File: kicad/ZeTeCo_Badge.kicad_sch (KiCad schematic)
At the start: 118 parts, among them J1 GPIO, J12 Bat. (+), J13 Bat. (-), J15 USB_A, J2 3V, Q1 2N7002, Q2 2N7002, Q3 2N7002, Q4 2N7002, U1 ATTINY85-20S

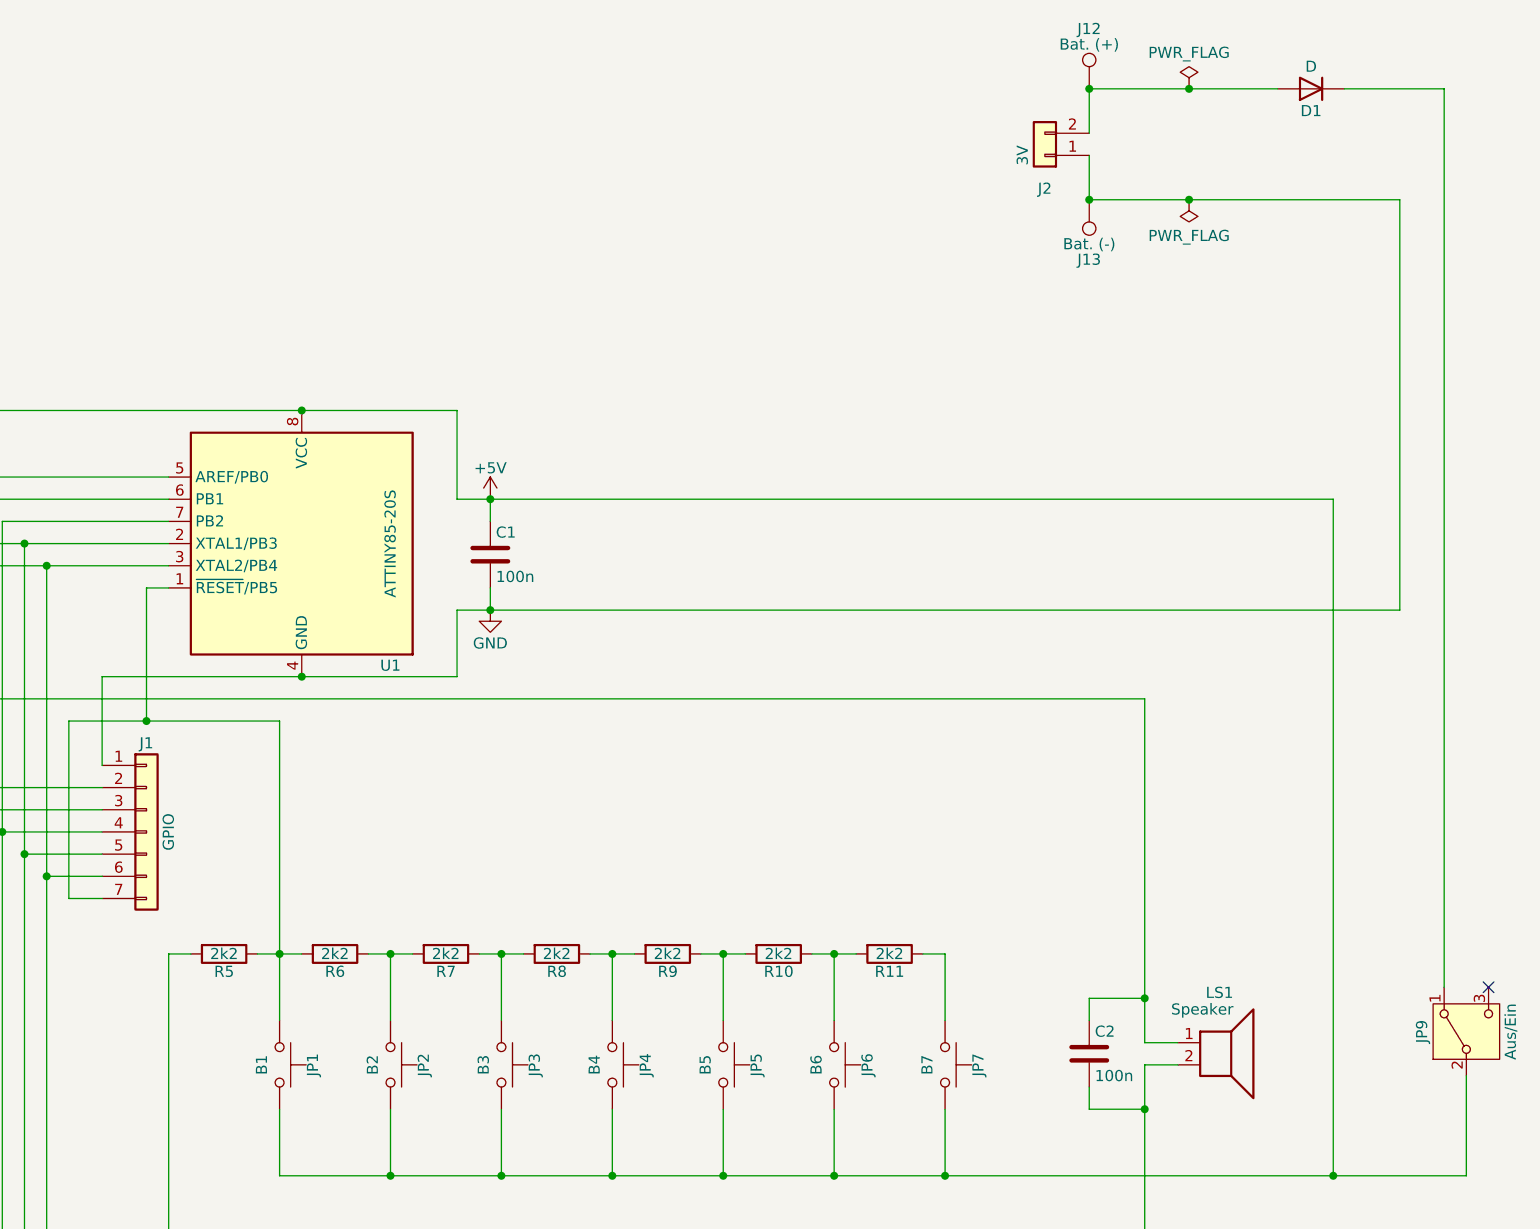
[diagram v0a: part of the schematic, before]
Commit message: Replace PCB text with component values on silkscreen
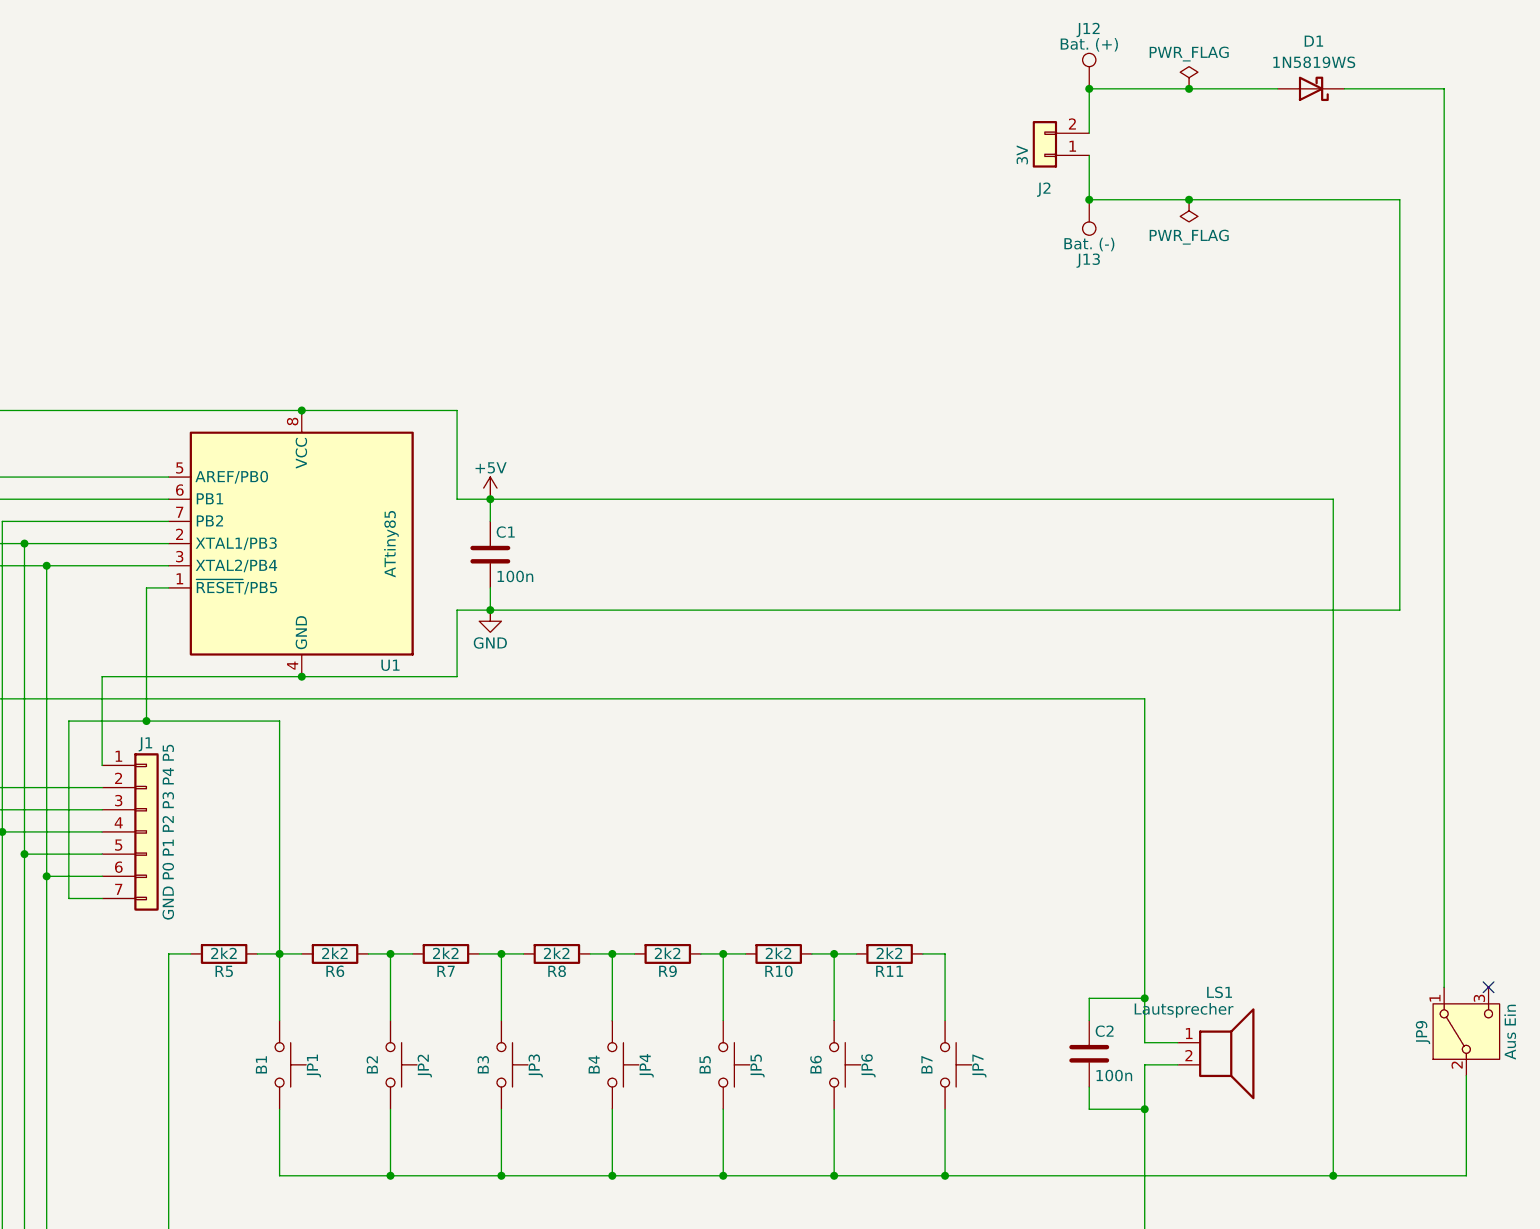
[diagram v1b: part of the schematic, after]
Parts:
- removed D1: D, Diode_SMD:D_1206_3216Metric_Pad1.42x1.75mm_HandSolder, symbol Device:D
- added D1: 1N5819WS, Diode_SMD:D_1206_3216Metric_Pad1.42x1.75mm_HandSolder, symbol Diode:1N5819WS
- J1: value GPIO -> GND P0 P1 P2 P3 P4 P5
- JP9: value Aus/Ein -> Aus Ein
- LS1: value Speaker -> Lautsprecher
- U1: value ATTINY85-20S -> ATtiny85
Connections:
- net at J12.1, J2.2 (Pin_2): now also D1.2 (A)
- net at JP9.1 (A): now also D1.1 (K)
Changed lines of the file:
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@@
 			)
 		)
-		(property "Value" "ATTINY85-20S"
+		(property "Value" "ATtiny85"
 			(at 267.97 83.82 90)
 			(effects
@@
 			)
 		)
-		(property "Value" "Speaker"
+		(property "Value" "Lautsprecher"
 			(at 364.49 137.16 0)
 			(effects
@@
 			)
 		)
-		(property "Value" "Aus/Ein"
+		(property "Value" "Aus    Ein"
 			(at 396.24 139.7 0)
 			(effects
@@
 	)
 	(symbol
-		(lib_id "Device:D")
-		(at 373.38 31.75 180)
-		(unit 1)
-		(exclude_from_sim no)
-		(in_bom yes)
-		(on_board yes)
-		(dnp no)
-		(property "Reference" "D1"
-			(at 373.38 34.29 0)
-			(effects
-				(font
-					(size 1.27 1.27)
-				)
-			)
-		)
-		(property "Value" "D"
-			(at 373.38 29.21 0)
-			(effects
-				(font
-					(size 1.27 1.27)
-				)
-			)
-		)
-		(property "Footprint" "Diode_SMD:D_1206_3216Metric_Pad1.42x1.75mm_HandSolder"
-			(at 373.38 31.75 0)
-			(effects
-				(font
-					(size 1.27 1.27)
-				)
-				(hide yes)
-			)
-		)
-		(property "Datasheet" ""
-			(at 373.38 31.75 0)
-			(effects
-				(font
-					(size 1.27 1.27)
-				)
-				(hide yes)
-			)
-		)
-		(property "Description" "Diode"
-			(at 373.38 31.75 0)
-			(effects
-				(font
-					(size 1.27 1.27)
-				)
-				(hide yes)
-			)
-		)
-		(property "Sim.Device" "D"
-			(at 373.38 31.75 0)
-			(effects
-				(font
-					(size 1.27 1.27)
-				)
-				(hide yes)
-			)
-		)
-		(property "Sim.Pins" "1=K 2=A"
-			(at 373.38 31.75 0)
-			(effects
-				(font
-					(size 1.27 1.27)
-				)
-				(hide yes)
-			)
-		)
-		(pin "2"
-		)
-		(pin "1"
-		)
-		(instances
-			(project ""
-				(path "/1ad60c3f-1b07-4916-ad93-138759b1bafa"
-					(reference "D1")
-					(unit 1)
-				)
-			)
-		)
-	)
-	(symbol
 		(lib_id "Device:C")
 		(at 279.4 85.09 0)
@@
 			)
 		)
-		(property "Value" "GPIO"
+		(property "Value" "GND P0 P1 P2 P3 P4 P5"
 			(at 242.57 116.84 90)
 			(effects
@@
 					(unit 1)
 				)
+			)
+		)
+	)
+	(symbol
+		(lib_id "Diode:1N5819WS")
+		(at 373.38 31.75 180)
+		(unit 1)
+		(exclude_from_sim no)
+		(in_bom yes)
+		(on_board yes)
+		(dnp no)
+		(fields_autoplaced yes)
+		(property "Reference" "D1"
+			(at 373.6975 26.3355 0)
+			(effects
+				(font
+					(size 1.27 1.27)
+				)
+			)
+		)
+		(property "Value" "1N5819WS"
+			(at 373.6975 28.7598 0)
+			(effects
+				(font
+					(size 1.27 1.27)
+				)
+			)
+		)
+		(property "Footprint" "Diode_SMD:D_1206_3216Metric_Pad1.42x1.75mm_HandSolder"
+			(at 373.38 27.305 0)
+			(effects
+				(font
+					(size 1.27 1.27)
+				)
+				(hide yes)
+			)
+		)
+		(property "Datasheet" "https://datasheet.lcsc.com/lcsc/2204281430_Guangdong-Hottech-1N5819WS_C191023.pdf"
+			(at 373.38 31.75 0)
+			(effects
+				(font
+					(size 1.27 1.27)
+				)
+				(hide yes)
+			)
+		)
+		(property "Description" "40V 600mV@1A 1A SOD-323 Schottky Barrier Diodes, SOD-323"
+			(at 373.38 31.75 0)
+			(effects
+				(font
+					(size 1.27 1.27)
+				)
+				(hide yes)
+			)
+		)
+		(pin "2"
+		)
+		(pin "1"
+		)
+		(instances
+			(project ""
+				(path "/1ad60c3f-1b07-4916-ad93-138759b1bafa"
+					(reference "D1")
+					(unit 1)
+				)
